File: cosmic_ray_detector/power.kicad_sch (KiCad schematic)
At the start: 16 parts

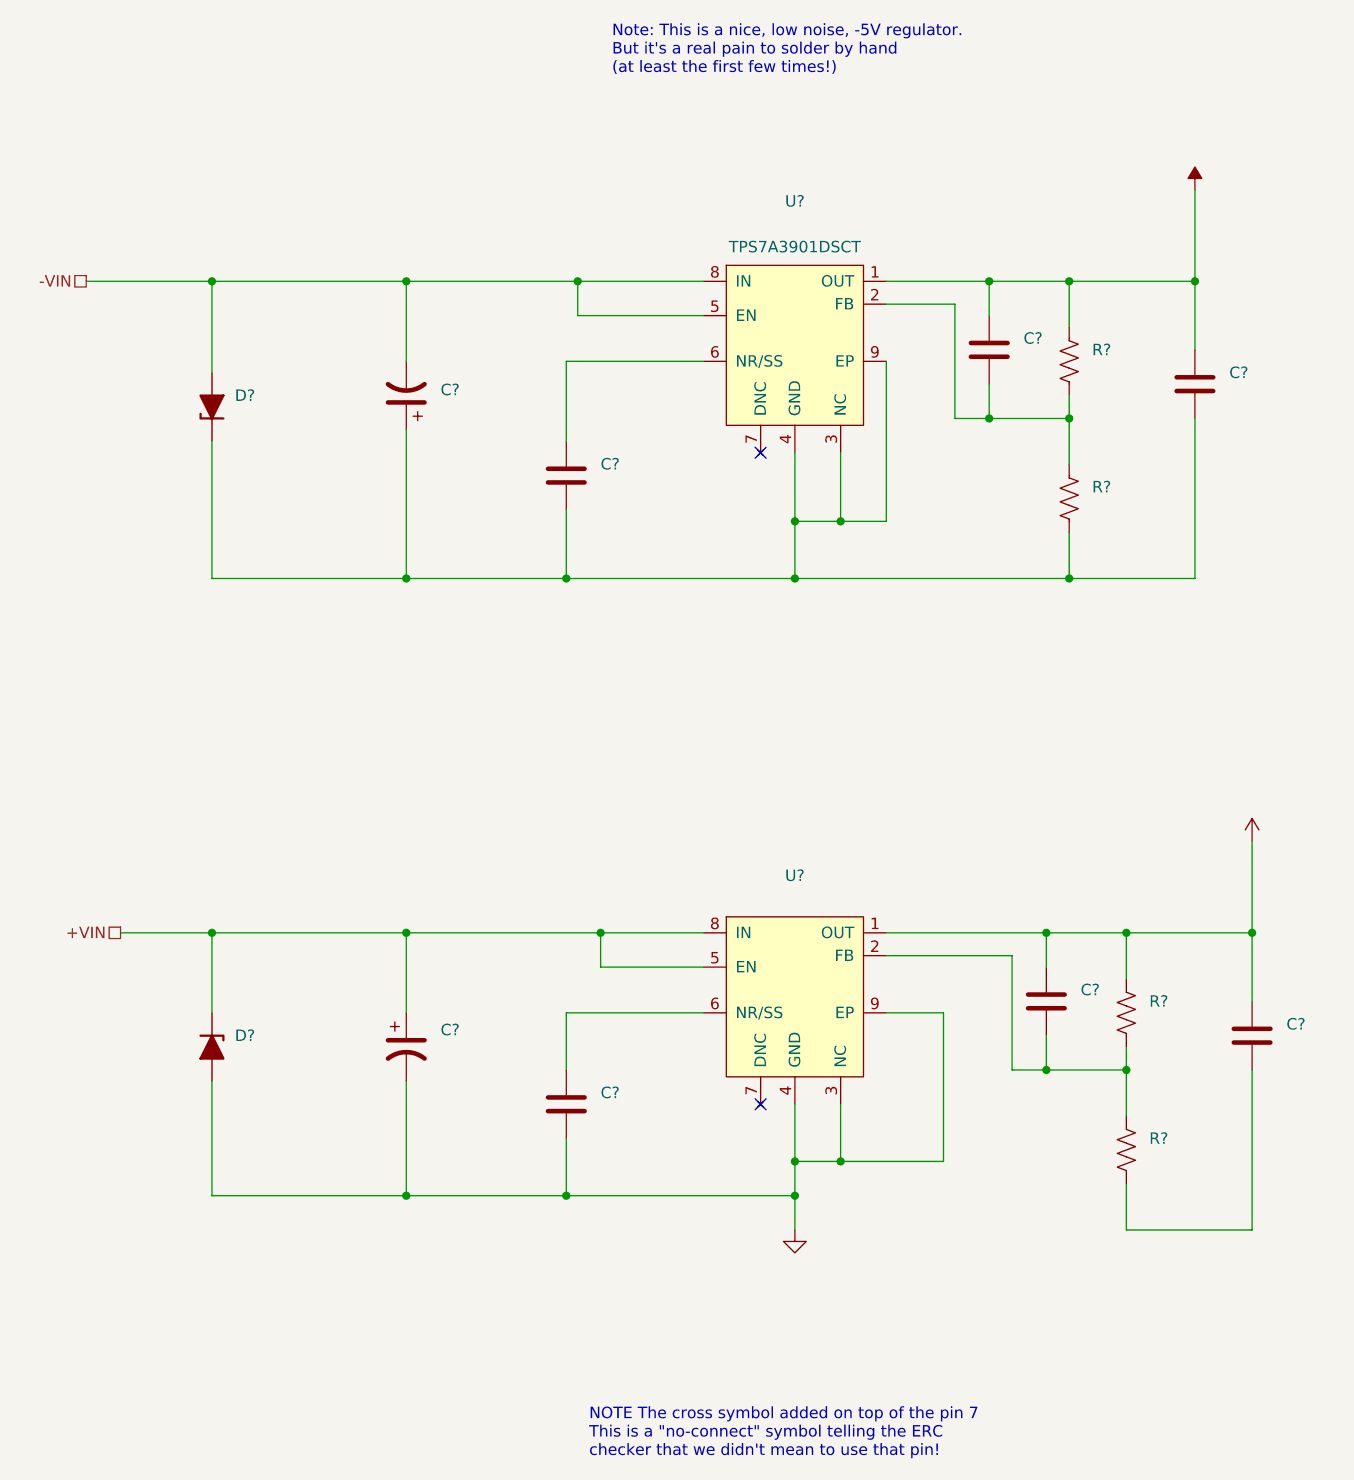
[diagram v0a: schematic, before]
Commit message: design of TLV3501 comparator sheet
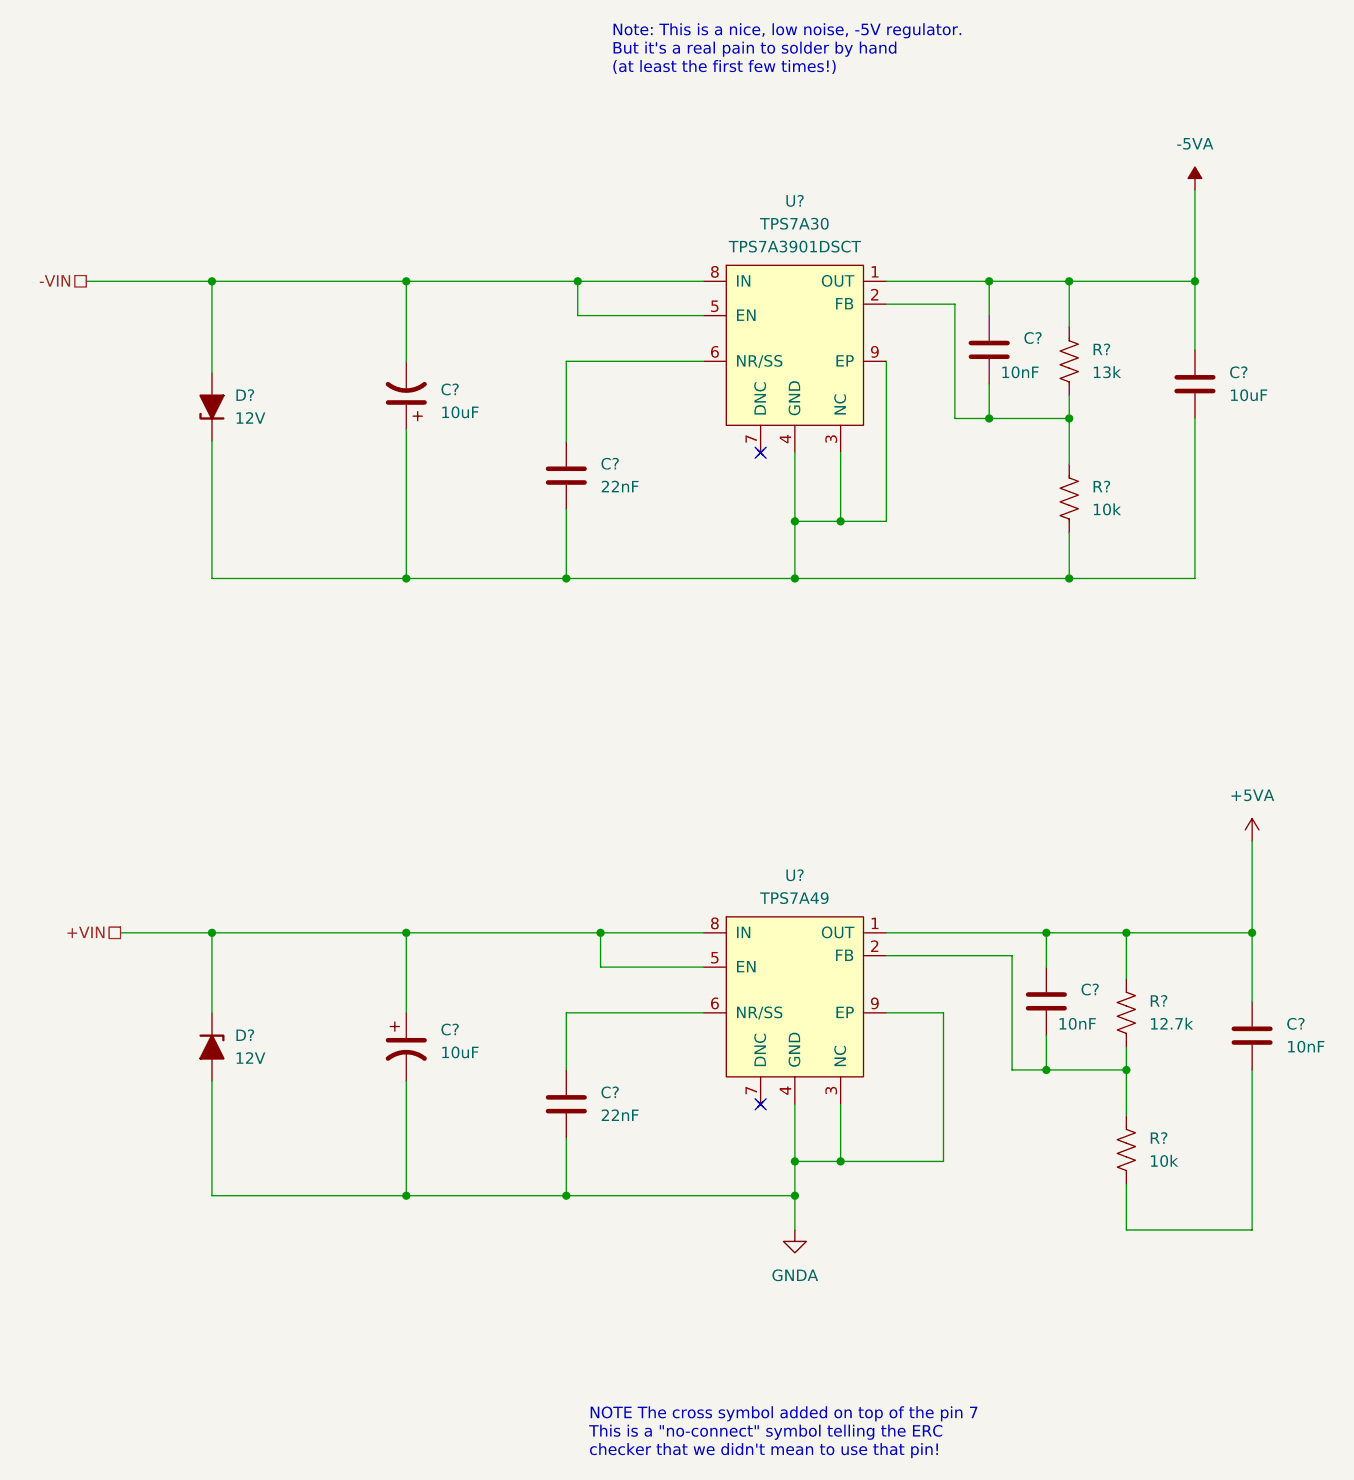
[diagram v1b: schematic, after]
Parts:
- C? (x3): value (none) -> 10uF
- C? (x3): value (none) -> 10nF
- C? (x2): value (none) -> 22nF
- D? (x2): value (none) -> 12V; footprint (none) -> Diode_SMD:D_SOD-123
- R? (x2): value (none) -> 10k
- R?: value (none) -> 12.7k
- R?: value (none) -> 13k
- U?: value (none) -> TPS7A30; footprint (none) -> SPIRIT:MSOP-8-1EP_3x3mm_P0.65mm_EP1.73x1.85mm_ThermalVias
- U?: value (none) -> TPS7A49; footprint (none) -> SPIRIT:MSOP-8-1EP_3x3mm_P0.65mm_EP1.73x1.85mm_ThermalVias
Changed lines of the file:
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@@
       (effects (font (size 1.27 1.27)) (justify left))
     )
-    (property "Value" "" (id 1) (at 165.1 149.8599 0)
+    (property "Value" "10k" (id 1) (at 165.1 149.8599 0)
       (effects (font (size 1.27 1.27)) (justify left))
     )
@@
       (effects (font (size 1.27 1.27)) (justify left))
     )
-    (property "Value" "" (id 1) (at 165.1 134.6199 0)
+    (property "Value" "12.7k" (id 1) (at 165.1 134.6199 0)
       (effects (font (size 1.27 1.27)) (justify left))
     )
@@
       (effects (font (size 1.27 1.27)) (justify left))
     )
-    (property "Value" "" (id 1) (at 86.36 137.7949 0)
+    (property "Value" "10uF" (id 1) (at 86.36 137.7949 0)
       (effects (font (size 1.27 1.27)) (justify left))
     )
@@
       (effects (font (size 1.27 1.27)) (justify left))
     )
-    (property "Value" "" (id 1) (at 180.34 137.1599 0)
+    (property "Value" "10nF" (id 1) (at 180.34 137.1599 0)
       (effects (font (size 1.27 1.27)) (justify left))
     )
@@
       (effects (font (size 1.27 1.27)) (justify left))
     )
-    (property "Value" "" (id 1) (at 158.75 62.2299 0)
+    (property "Value" "13k" (id 1) (at 158.75 62.2299 0)
       (effects (font (size 1.27 1.27)) (justify left))
     )
@@
       (effects (font (size 1.27 1.27)) (justify left))
     )
-    (property "Value" "" (id 1) (at 158.75 77.4699 0)
+    (property "Value" "10k" (id 1) (at 158.75 77.4699 0)
       (effects (font (size 1.27 1.27)) (justify left))
     )
@@
       (effects (font (size 1.27 1.27)) (justify left))
     )
-    (property "Value" "" (id 1) (at 154.94 134.62 0)
+    (property "Value" "10nF" (id 1) (at 154.94 134.62 0)
       (effects (font (size 1.27 1.27)) (justify left))
     )
@@
       (effects (font (size 1.27 1.27)) hide)
     )
-    (property "Value" "" (id 1) (at 170.18 36.83 0))
+    (property "Value" "-5VA" (id 1) (at 170.18 36.83 0))
     (property "Footprint" "" (id 2) (at 170.18 41.91 0)
       (effects (font (size 1.27 1.27)) hide)
@@
       (effects (font (size 1.27 1.27)) (justify left))
     )
-    (property "Value" "" (id 1) (at 104.14 74.9299 0)
+    (property "Value" "22nF" (id 1) (at 104.14 74.9299 0)
       (effects (font (size 1.27 1.27)) (justify left))
     )
@@
       (effects (font (size 1.27 1.27)) hide)
     )
-    (property "Value" "" (id 1) (at 125.73 162.56 0))
+    (property "Value" "GNDA" (id 1) (at 125.73 162.56 0))
     (property "Footprint" "" (id 2) (at 125.73 157.48 0)
       (effects (font (size 1.27 1.27)) hide)
@@
       (effects (font (size 1.27 1.27)) (justify left))
     )
-    (property "Value" "" (id 1) (at 63.5 138.4299 90)
-      (effects (font (size 1.27 1.27)) (justify left))
-    )
-    (property "Footprint" "" (id 2) (at 60.96 137.16 0)
+    (property "Value" "12V" (id 1) (at 63.5 138.4299 90)
+      (effects (font (size 1.27 1.27)) (justify left))
+    )
+    (property "Footprint" "Diode_SMD:D_SOD-123" (id 2) (at 60.96 137.16 0)
       (effects (font (size 1.27 1.27)) hide)
     )
@@
     (in_bom yes) (on_board yes) (fields_autoplaced)
     (property "Reference" "U?" (id 0) (at 125.73 43.18 0))
-    (property "Value" "" (id 1) (at 125.73 45.72 0))
-    (property "Footprint" "" (id 2) (at 125.73 54.61 0)
+    (property "Value" "TPS7A30" (id 1) (at 125.73 45.72 0))
+    (property "Footprint" "SPIRIT:MSOP-8-1EP_3x3mm_P0.65mm_EP1.73x1.85mm_ThermalVias" (id 2) (at 125.73 54.61 0)
       (effects (font (size 1.27 1.27)) hide)
     )
@@
       (effects (font (size 1.27 1.27)) (justify left))
     )
-    (property "Value" "" (id 1) (at 173.99 64.7699 0)
+    (property "Value" "10uF" (id 1) (at 173.99 64.7699 0)
       (effects (font (size 1.27 1.27)) (justify left))
     )
@@
     (in_bom yes) (on_board yes) (fields_autoplaced)
     (property "Reference" "U?" (id 0) (at 125.73 118.11 0))
-    (property "Value" "" (id 1) (at 125.73 120.65 0))
-    (property "Footprint" "" (id 2) (at 125.73 127 0)
+    (property "Value" "TPS7A49" (id 1) (at 125.73 120.65 0))
+    (property "Footprint" "SPIRIT:MSOP-8-1EP_3x3mm_P0.65mm_EP1.73x1.85mm_ThermalVias" (id 2) (at 125.73 127 0)
       (effects (font (size 1.27 1.27)) hide)
     )
@@
       (effects (font (size 1.27 1.27)) (justify left))
     )
-    (property "Value" "" (id 1) (at 104.14 144.7799 0)
+    (property "Value" "22nF" (id 1) (at 104.14 144.7799 0)
       (effects (font (size 1.27 1.27)) (justify left))
     )
@@
       (effects (font (size 1.27 1.27)) (justify right))
     )
-    (property "Value" "" (id 1) (at 63.5 67.3099 90)
+    (property "Value" "12V" (id 1) (at 63.5 67.3099 90)
       (effects (font (size 1.27 1.27)) (justify right))
     )
-    (property "Footprint" "" (id 2) (at 60.96 66.04 0)
+    (property "Footprint" "Diode_SMD:D_SOD-123" (id 2) (at 60.96 66.04 0)
       (effects (font (size 1.27 1.27)) hide)
     )
@@
       (effects (font (size 1.27 1.27)) (justify left))
     )
-    (property "Value" "" (id 1) (at 148.59 62.23 0)
+    (property "Value" "10nF" (id 1) (at 148.59 62.23 0)
       (effects (font (size 1.27 1.27)) (justify left))
     )
@@
       (effects (font (size 1.27 1.27)) (justify right))
     )
-    (property "Value" "" (id 1) (at 86.36 66.6749 0)
+    (property "Value" "10uF" (id 1) (at 86.36 66.6749 0)
       (effects (font (size 1.27 1.27)) (justify right))
     )
@@
       (effects (font (size 1.27 1.27)) hide)
     )
-    (property "Value" "" (id 1) (at 176.53 109.22 0))
+    (property "Value" "+5VA" (id 1) (at 176.53 109.22 0))
     (property "Footprint" "" (id 2) (at 176.53 114.3 0)
       (effects (font (size 1.27 1.27)) hide)

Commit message: annotated schematic
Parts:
- gave numbers to parts that had none: 16
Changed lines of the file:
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@@
   (symbol (lib_id "Device:R_US") (at 162.56 148.59 0) (unit 1)
     (in_bom yes) (on_board yes) (fields_autoplaced)
-    (property "Reference" "R?" (id 0) (at 165.1 147.3199 0)
+    (property "Reference" "R8" (id 0) (at 165.1 147.3199 0)
       (effects (font (size 1.27 1.27)) (justify left))
     )
@@
   (symbol (lib_id "Device:R_US") (at 162.56 133.35 0) (unit 1)
     (in_bom yes) (on_board yes) (fields_autoplaced)
-    (property "Reference" "R?" (id 0) (at 165.1 132.0799 0)
+    (property "Reference" "R7" (id 0) (at 165.1 132.0799 0)
       (effects (font (size 1.27 1.27)) (justify left))
     )
@@
   (symbol (lib_id "Device:C_Polarized_US") (at 82.55 137.16 0) (unit 1)
     (in_bom yes) (on_board yes) (fields_autoplaced)
-    (property "Reference" "C?" (id 0) (at 86.36 135.2549 0)
+    (property "Reference" "C10" (id 0) (at 86.36 135.2549 0)
       (effects (font (size 1.27 1.27)) (justify left))
     )
@@
   (symbol (lib_id "Device:C") (at 176.53 135.89 0) (unit 1)
     (in_bom yes) (on_board yes) (fields_autoplaced)
-    (property "Reference" "C?" (id 0) (at 180.34 134.6199 0)
+    (property "Reference" "C16" (id 0) (at 180.34 134.6199 0)
       (effects (font (size 1.27 1.27)) (justify left))
     )
@@
   (symbol (lib_id "Device:R_US") (at 156.21 60.96 0) (unit 1)
     (in_bom yes) (on_board yes) (fields_autoplaced)
-    (property "Reference" "R?" (id 0) (at 158.75 59.6899 0)
+    (property "Reference" "R5" (id 0) (at 158.75 59.6899 0)
       (effects (font (size 1.27 1.27)) (justify left))
     )
@@
   (symbol (lib_id "Device:R_US") (at 156.21 76.2 0) (unit 1)
     (in_bom yes) (on_board yes) (fields_autoplaced)
-    (property "Reference" "R?" (id 0) (at 158.75 74.9299 0)
+    (property "Reference" "R6" (id 0) (at 158.75 74.9299 0)
       (effects (font (size 1.27 1.27)) (justify left))
     )
@@
   (symbol (lib_id "Device:C") (at 153.67 132.08 0) (unit 1)
     (in_bom yes) (on_board yes)
-    (property "Reference" "C?" (id 0) (at 157.48 130.8099 0)
+    (property "Reference" "C14" (id 0) (at 157.48 130.8099 0)
       (effects (font (size 1.27 1.27)) (justify left))
     )
@@
   (symbol (lib_id "power:-5VA") (at 170.18 41.91 0) (unit 1)
     (in_bom yes) (on_board yes) (fields_autoplaced)
-    (property "Reference" "#PWR?" (id 0) (at 170.18 39.37 0)
+    (property "Reference" "#PWR013" (id 0) (at 170.18 39.37 0)
       (effects (font (size 1.27 1.27)) hide)
     )
@@
   (symbol (lib_id "Device:C") (at 100.33 73.66 0) (unit 1)
     (in_bom yes) (on_board yes) (fields_autoplaced)
-    (property "Reference" "C?" (id 0) (at 104.14 72.3899 0)
+    (property "Reference" "C11" (id 0) (at 104.14 72.3899 0)
       (effects (font (size 1.27 1.27)) (justify left))
     )
@@
   (symbol (lib_id "power:GNDA") (at 125.73 157.48 0) (unit 1)
     (in_bom yes) (on_board yes) (fields_autoplaced)
-    (property "Reference" "#PWR?" (id 0) (at 125.73 163.83 0)
+    (property "Reference" "#PWR012" (id 0) (at 125.73 163.83 0)
       (effects (font (size 1.27 1.27)) hide)
     )
@@
   (symbol (lib_id "Device:D_Zener_Filled") (at 60.96 137.16 270) (unit 1)
     (in_bom yes) (on_board yes) (fields_autoplaced)
-    (property "Reference" "D?" (id 0) (at 63.5 135.8899 90)
+    (property "Reference" "D3" (id 0) (at 63.5 135.8899 90)
       (effects (font (size 1.27 1.27)) (justify left))
     )
@@
   (symbol (lib_id "cosmic_ray_symbols:TPS7A30") (at 125.73 54.61 0) (unit 1)
     (in_bom yes) (on_board yes) (fields_autoplaced)
-    (property "Reference" "U?" (id 0) (at 125.73 43.18 0))
+    (property "Reference" "U2" (id 0) (at 125.73 43.18 0))
     (property "Value" "TPS7A30" (id 1) (at 125.73 45.72 0))
     (property "Footprint" "SPIRIT:MSOP-8-1EP_3x3mm_P0.65mm_EP1.73x1.85mm_ThermalVias" (id 2) (at 125.73 54.61 0)
@@
   (symbol (lib_id "Device:C") (at 170.18 63.5 0) (unit 1)
     (in_bom yes) (on_board yes) (fields_autoplaced)
-    (property "Reference" "C?" (id 0) (at 173.99 62.2299 0)
+    (property "Reference" "C15" (id 0) (at 173.99 62.2299 0)
       (effects (font (size 1.27 1.27)) (justify left))
     )
@@
   (symbol (lib_id "cosmic_ray_symbols:TPS7A49") (at 125.73 127 0) (unit 1)
     (in_bom yes) (on_board yes) (fields_autoplaced)
-    (property "Reference" "U?" (id 0) (at 125.73 118.11 0))
+    (property "Reference" "U3" (id 0) (at 125.73 118.11 0))
     (property "Value" "TPS7A49" (id 1) (at 125.73 120.65 0))
     (property "Footprint" "SPIRIT:MSOP-8-1EP_3x3mm_P0.65mm_EP1.73x1.85mm_ThermalVias" (id 2) (at 125.73 127 0)
@@
   (symbol (lib_id "Device:C") (at 100.33 143.51 0) (unit 1)
     (in_bom yes) (on_board yes) (fields_autoplaced)
-    (property "Reference" "C?" (id 0) (at 104.14 142.2399 0)
+    (property "Reference" "C12" (id 0) (at 104.14 142.2399 0)
       (effects (font (size 1.27 1.27)) (justify left))
     )
@@
   (symbol (lib_id "Device:D_Zener_Filled") (at 60.96 66.04 90) (unit 1)
     (in_bom yes) (on_board yes) (fields_autoplaced)
-    (property "Reference" "D?" (id 0) (at 63.5 64.7699 90)
+    (property "Reference" "D2" (id 0) (at 63.5 64.7699 90)
       (effects (font (size 1.27 1.27)) (justify right))
     )
@@
   (symbol (lib_id "Device:C") (at 147.32 59.69 0) (unit 1)
     (in_bom yes) (on_board yes)
-    (property "Reference" "C?" (id 0) (at 151.13 58.4199 0)
+    (property "Reference" "C13" (id 0) (at 151.13 58.4199 0)
       (effects (font (size 1.27 1.27)) (justify left))
     )
@@
   (symbol (lib_id "Device:C_Polarized_US") (at 82.55 64.77 180) (unit 1)
     (in_bom yes) (on_board yes) (fields_autoplaced)
-    (property "Reference" "C?" (id 0) (at 86.36 64.1349 0)
+    (property "Reference" "C9" (id 0) (at 86.36 64.1349 0)
       (effects (font (size 1.27 1.27)) (justify right))
     )
@@
   (symbol (lib_id "power:+5VA") (at 176.53 114.3 0) (unit 1)
     (in_bom yes) (on_board yes) (fields_autoplaced)
-    (property "Reference" "#PWR?" (id 0) (at 176.53 118.11 0)
-      (effects (font (size 1.27 1.27)) hide)
-    )
+    (property "Reference" "#PWR014" (id 0) (at 176.53 118.11 0)
+      (effects (font (size 1.27 1.27)) hide)
+    )
